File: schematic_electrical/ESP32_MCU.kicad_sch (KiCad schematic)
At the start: 14 parts, among them U1 ESP32_S2_PICO

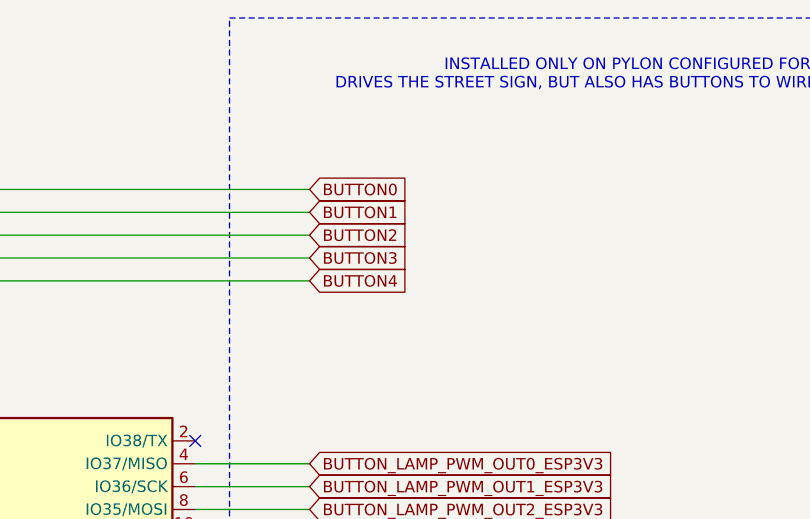
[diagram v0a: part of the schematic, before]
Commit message: Schematic options for bar placement bar box (button controller)
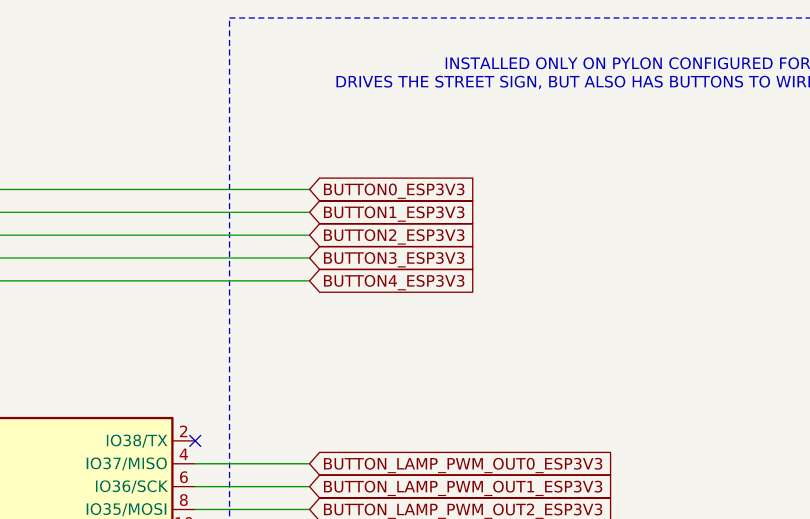
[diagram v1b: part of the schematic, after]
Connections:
- net BUTTON0 renamed BUTTON0_ESP3V3
- net BUTTON1 renamed BUTTON1_ESP3V3
- net BUTTON2 renamed BUTTON2_ESP3V3
- net BUTTON3 renamed BUTTON3_ESP3V3
- net BUTTON4 renamed BUTTON4_ESP3V3
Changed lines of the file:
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@@
 		)
 	)
-	(global_label "BUTTON1"
+	(global_label "BUTTON1_ESP3V3"
 		(shape input)
 		(at 193.04 35.56 0)
@@
 		)
 	)
-	(global_label "BUTTON4"
+	(global_label "BUTTON4_ESP3V3"
 		(shape input)
 		(at 193.04 43.18 0)
@@
 		)
 	)
-	(global_label "BUTTON2"
+	(global_label "BUTTON2_ESP3V3"
 		(shape input)
 		(at 193.04 38.1 0)
@@
 		)
 	)
-	(global_label "BUTTON3"
+	(global_label "BUTTON3_ESP3V3"
 		(shape input)
 		(at 193.04 40.64 0)
@@
 		)
 	)
-	(global_label "BUTTON0"
+	(global_label "BUTTON0_ESP3V3"
 		(shape input)
 		(at 193.04 33.02 0)
